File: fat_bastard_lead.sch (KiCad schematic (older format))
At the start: 33 parts, among them J1 HT IN, J2 LD_IN, J3 12V_IN, J4 GAIN, J5 LD_OUT, U1 ECC83, U2 ECC83

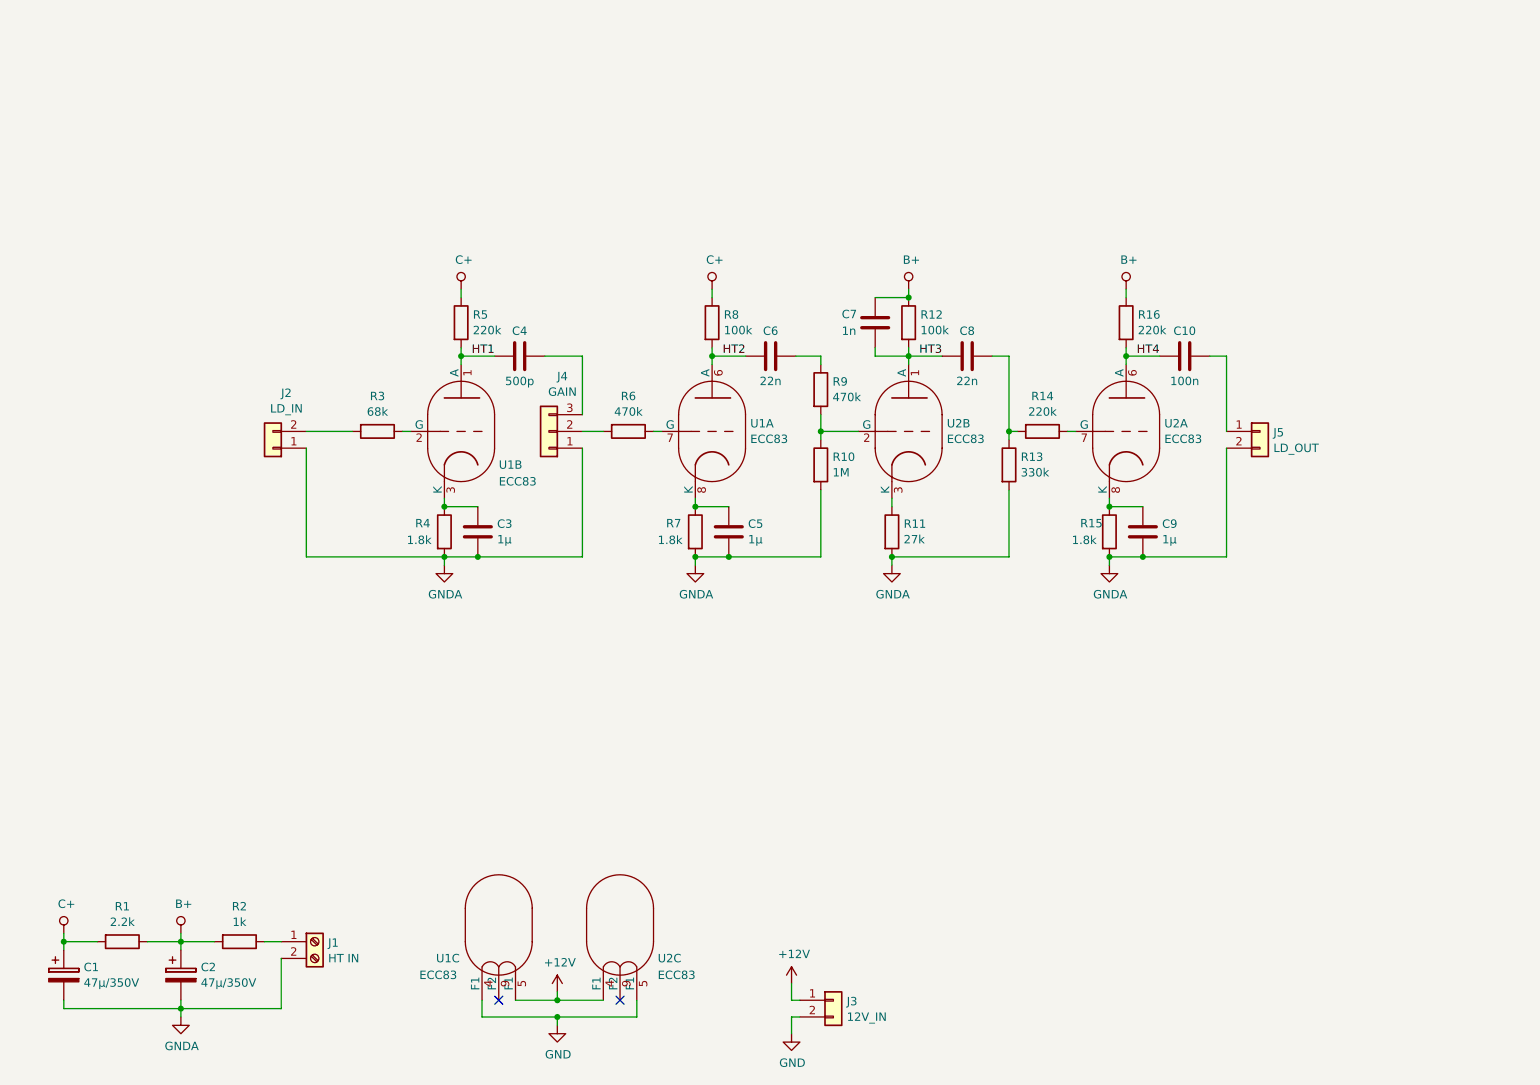
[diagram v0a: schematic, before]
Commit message: Route lead channel PCB
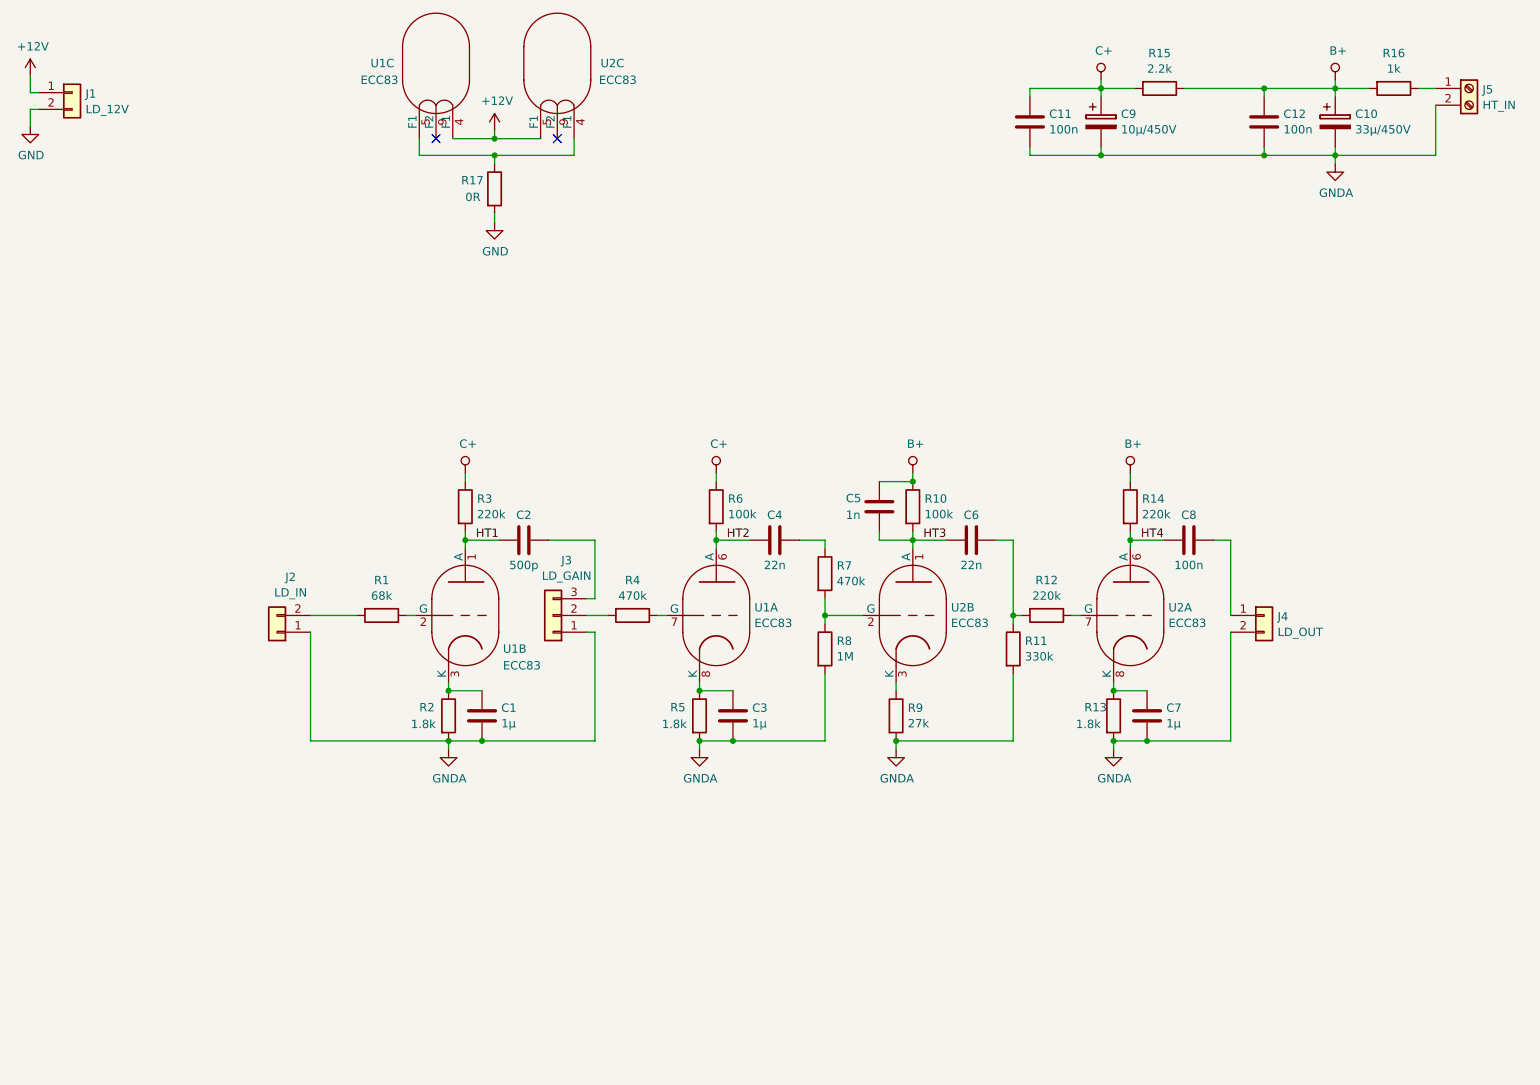
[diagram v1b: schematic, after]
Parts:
- removed C1, C2: 47µ/350V, Capacitor_THT:C_Axial_L22.0mm_D10.5mm_P27.50mm_Horizontal, symbol Device:CP
- removed C10: 100n, Capacitor_THT:C_Rect_L7.0mm_W2.5mm_P5.00mm, symbol Device:C
- removed C9: 1µ, Capacitor_THT:C_Rect_L7.0mm_W3.5mm_P5.00mm, symbol Device:C
- removed J1: HT IN, TerminalBlock:TerminalBlock_bornier-2_P5.08mm, symbol Connector:Screw_Terminal_01x02
- removed J3: 12V_IN, Connector_PinHeader_2.54mm:PinHeader_1x02_P2.54mm_Horizontal, symbol Connector_Generic:Conn_01x02
- removed J4: GAIN, Connector_PinHeader_2.54mm:PinHeader_1x03_P2.54mm_Vertical, symbol Connector_Generic:Conn_01x03
- removed J5: LD_OUT, Connector_PinHeader_2.54mm:PinHeader_1x02_P2.54mm_Horizontal, symbol Connector_Generic:Conn_01x02
- added C1: 1µ, Capacitor_THT:C_Rect_L7.2mm_W4.5mm_P5.00mm_FKS2_FKP2_MKS2_MKP2, symbol Device:C
- added C10: 33µ/450V, Capacitor_THT:CP_Radial_D16.0mm_P7.50mm, symbol Device:CP
- added C11, C12: 100n, Capacitor_THT:C_Rect_L19.0mm_W6.0mm_P15.00mm_MKS4, symbol Device:C
- added C2: 500p, Capacitor_THT:C_Rect_L10.0mm_W5.0mm_P5.00mm_P7.50mm, symbol Device:C
- added C9: 10µ/450V, Capacitor_THT:CP_Radial_D13.0mm_P5.00mm, symbol Device:CP
- added J1: LD_12V, Connector_PinHeader_2.54mm:PinHeader_1x02_P2.54mm_Horizontal, symbol Connector_Generic:Conn_01x02
- added J3: LD_GAIN, Connector_PinHeader_2.54mm:PinHeader_1x03_P2.54mm_Vertical, symbol Connector_Generic:Conn_01x03
- added J4: LD_OUT, Connector_PinHeader_2.54mm:PinHeader_1x02_P2.54mm_Horizontal, symbol Connector_Generic:Conn_01x02
- added J5: HT_IN, TerminalBlock_RND:TerminalBlock_RND_205-00001_1x02_P5.00mm_Horizontal, symbol Connector:Screw_Terminal_01x02
- added R17: 0R, Jumper:SolderJumper-2_P1.3mm_Bridged2Bar_Pad1.0x1.5mm, symbol Device:R
- C3: footprint Capacitor_THT:C_Rect_L7.0mm_W2.5mm_P5.00mm -> Capacitor_THT:C_Rect_L7.2mm_W4.5mm_P5.00mm_FKS2_FKP2_MKS2_MKP2
- C4: value 500p -> 22n; footprint Capacitor_THT:C_Rect_L7.0mm_W2.5mm_P5.00mm -> Capacitor_THT:C_Rect_L13.0mm_W4.0mm_P10.00mm_FKS3_FKP3_MKS4
- C5: value 1µ -> 1n; footprint Capacitor_THT:C_Rect_L7.0mm_W3.5mm_P5.00mm -> Capacitor_THT:C_Rect_L10.0mm_W3.0mm_P7.50mm_MKS4
- C6: footprint Capacitor_THT:C_Rect_L7.0mm_W2.5mm_P5.00mm -> Capacitor_THT:C_Rect_L13.0mm_W4.0mm_P10.00mm_FKS3_FKP3_MKS4
- C7: value 1n -> 1µ; footprint Capacitor_THT:C_Rect_L7.0mm_W2.5mm_P5.00mm -> Capacitor_THT:C_Rect_L7.2mm_W4.5mm_P5.00mm_FKS2_FKP2_MKS2_MKP2
- C8: value 22n -> 100n; footprint Capacitor_THT:C_Rect_L7.0mm_W3.5mm_P5.00mm -> Capacitor_THT:C_Rect_L19.0mm_W6.0mm_P15.00mm_MKS4
- R1: value 2.2k -> 68k; footprint Resistor_THT:R_Axial_DIN0207_L6.3mm_D2.5mm_P7.62mm_Horizontal -> Resistor_THT:R_Axial_DIN0309_L9.0mm_D3.2mm_P12.70mm_Horizontal
- R10: value 1M -> 100k; footprint Resistor_THT:R_Axial_DIN0207_L6.3mm_D2.5mm_P7.62mm_Horizontal -> Resistor_THT:R_Axial_DIN0309_L9.0mm_D3.2mm_P12.70mm_Horizontal
- R11: value 27k -> 330k; footprint Resistor_THT:R_Axial_DIN0207_L6.3mm_D2.5mm_P7.62mm_Horizontal -> Resistor_THT:R_Axial_DIN0309_L9.0mm_D3.2mm_P12.70mm_Horizontal
- R12: value 100k -> 220k; footprint Resistor_THT:R_Axial_DIN0207_L6.3mm_D2.5mm_P7.62mm_Horizontal -> Resistor_THT:R_Axial_DIN0309_L9.0mm_D3.2mm_P12.70mm_Horizontal
- R13: value 330k -> 1.8k; footprint Resistor_THT:R_Axial_DIN0207_L6.3mm_D2.5mm_P7.62mm_Horizontal -> Resistor_THT:R_Axial_DIN0309_L9.0mm_D3.2mm_P12.70mm_Horizontal
- R14: footprint Resistor_THT:R_Axial_DIN0207_L6.3mm_D2.5mm_P7.62mm_Horizontal -> Resistor_THT:R_Axial_DIN0309_L9.0mm_D3.2mm_P12.70mm_Horizontal
- R15: value 1.8k -> 2.2k; footprint Resistor_THT:R_Axial_DIN0207_L6.3mm_D2.5mm_P7.62mm_Horizontal -> Resistor_THT:R_Axial_DIN0309_L9.0mm_D3.2mm_P12.70mm_Horizontal
- R16: value 220k -> 1k; footprint Resistor_THT:R_Axial_DIN0207_L6.3mm_D2.5mm_P7.62mm_Horizontal -> Resistor_THT:R_Axial_DIN0309_L9.0mm_D3.2mm_P12.70mm_Horizontal
- R2: value 1k -> 1.8k; footprint Resistor_THT:R_Axial_DIN0207_L6.3mm_D2.5mm_P7.62mm_Horizontal -> Resistor_THT:R_Axial_DIN0309_L9.0mm_D3.2mm_P12.70mm_Horizontal
- R3: value 68k -> 220k; footprint Resistor_THT:R_Axial_DIN0207_L6.3mm_D2.5mm_P7.62mm_Horizontal -> Resistor_THT:R_Axial_DIN0309_L9.0mm_D3.2mm_P12.70mm_Horizontal
- R4, R7: value 1.8k -> 470k; footprint Resistor_THT:R_Axial_DIN0207_L6.3mm_D2.5mm_P7.62mm_Horizontal -> Resistor_THT:R_Axial_DIN0309_L9.0mm_D3.2mm_P12.70mm_Horizontal
- R5: value 220k -> 1.8k; footprint Resistor_THT:R_Axial_DIN0207_L6.3mm_D2.5mm_P7.62mm_Horizontal -> Resistor_THT:R_Axial_DIN0309_L9.0mm_D3.2mm_P12.70mm_Horizontal
- R6: value 470k -> 100k; footprint Resistor_THT:R_Axial_DIN0207_L6.3mm_D2.5mm_P7.62mm_Horizontal -> Resistor_THT:R_Axial_DIN0309_L9.0mm_D3.2mm_P12.70mm_Horizontal
- R8: value 100k -> 1M; footprint Resistor_THT:R_Axial_DIN0207_L6.3mm_D2.5mm_P7.62mm_Horizontal -> Resistor_THT:R_Axial_DIN0309_L9.0mm_D3.2mm_P12.70mm_Horizontal
- R9: value 470k -> 27k; footprint Resistor_THT:R_Axial_DIN0207_L6.3mm_D2.5mm_P7.62mm_Horizontal -> Resistor_THT:R_Axial_DIN0309_L9.0mm_D3.2mm_P12.70mm_Horizontal
- U1, U2: footprint Valve:Valve_Noval_P -> Valve:Valve_ECC-83-2
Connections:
- net +12V: now also U1.4 (F1), U2.5 (F1), J1.1 (Pin_1); no longer U1.5 (F1), U2.4 (F1)
- net B+: now also C5.1, R10.1, R14.1, R15.1, R16.2, C10.1, C12.2; no longer C7.1, R1.1, R12.1, R16.1, R2.2
- net C+: now also R15.2, R3.1, R6.1, C11.2, C9.1; no longer R1.2, R5.1, R8.1
- net GND: now also J1.2 (Pin_2), R17.2; no longer U1.4 (F1), U2.5 (F1)
- net GNDA: now also C7.1, R2.2, R5.2, R8.2, R9.2, C1.1, C10.2, C11.1, C12.1, C9.2, J3.1 (Pin_1), J4.2 (Pin_2), J5.2 (Pin_2); no longer C5.1, R10.2, R15.2, R4.2, R7.2
- net HT1: now also R3.2, C2.2; no longer C4.2, R5.2
- net HT2: now also C4.2, R6.2; no longer C6.2, R8.2
- net HT3: now also C5.2, C6.2, R10.2; no longer C7.2, C8.2, R12.2
- net HT4: now also C8.2, R14.2; no longer R16.2
- net at U1.2 (G): now also R1.1; no longer R3.1
- net at U2.3 (K): now also R9.1; no longer R11.1
- net at U1.7 (G): now also R4.1; no longer R6.1
- net at U2.7 (G): now also R12.1; no longer R14.1
- net at U2.8 (K): now also C7.2, R13.1; no longer R15.1
- net at C4.1: now also R7.1
- net at R2.1: now also U1.3 (K), C1.2
- net at J2.2 (Pin_2): now also R1.2; no longer R3.2
- net at C6.1: now also R11.1, R12.2; no longer R9.1
- new net: R7.2, R8.1, U2.2 (G)
- new net: C3.2, R5.1, U1.8 (K)
- new net: C2.1, J3.3 (Pin_3)
- new net: J5.1 (Pin_1), R16.1
- new net: J3.2 (Pin_2), R4.2
- new net: C8.1, J4.1 (Pin_1)
- new net: R17.1, U1.5 (F1), U2.4 (F1)
